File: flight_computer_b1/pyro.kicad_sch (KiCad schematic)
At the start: 11 parts, among them Q1 MMBT3904, Q2 PMOS, U11 IRLML6344TRPBF

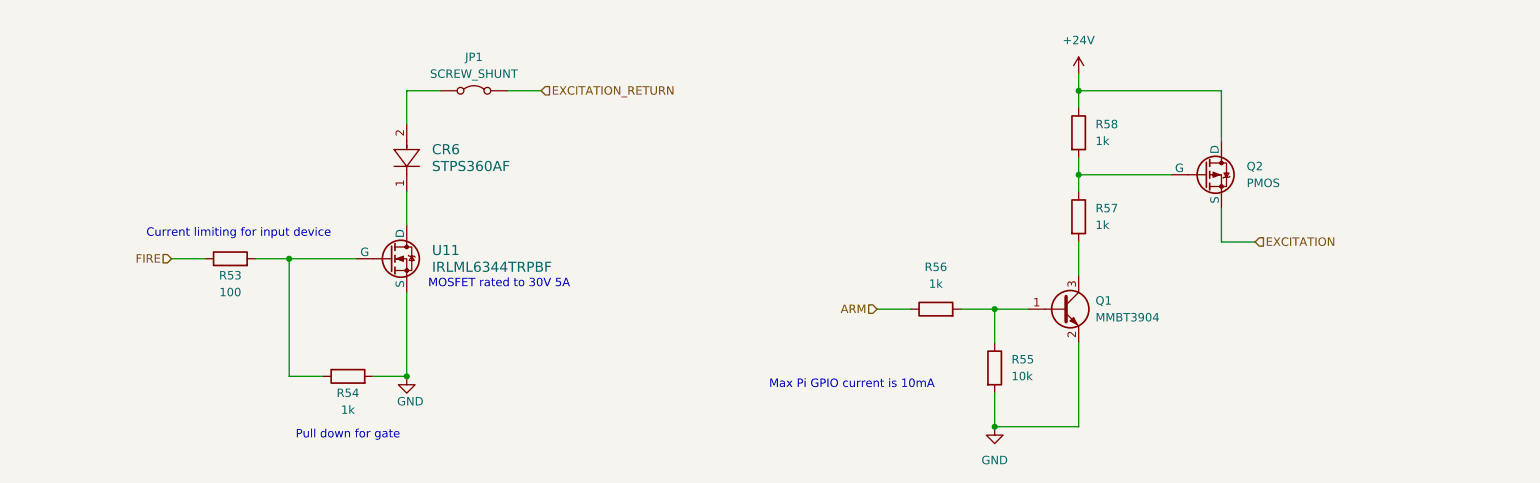
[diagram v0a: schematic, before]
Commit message: flight computer: new ideal diode, small schematic changes
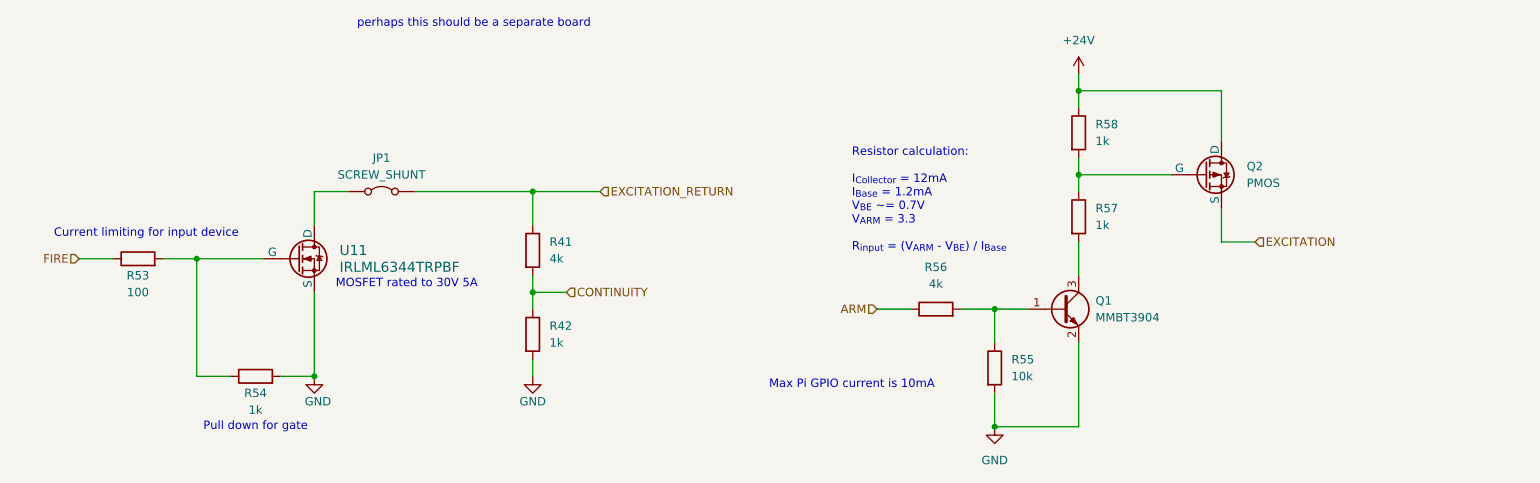
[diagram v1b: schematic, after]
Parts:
- removed CR6: STPS360AF, Diode_SMD:D_SOD-128, symbol MBRS360T3G:MBRS360T3G
- added R41: 4k, Resistor_SMD:R_0603_1608Metric, symbol Device:R
- added R42: 1k, Resistor_SMD:R_0603_1608Metric, symbol Device:R
- R56: value 1k -> 4k
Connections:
- net EXCITATION_RETURN: now also R41.1
- net GND: now also R42.2
- net at U11.1 (D): now also JP1.1 (A)
- new net CONTINUITY: R41.2, R42.1
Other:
- note added: "Resistor calculation: I_{Collector} = 12mA I_{Base} = 1.2mA V_{BE} ~= 0.7V V_{ARM} = 3.3 R_{input} = (V_{ARM} - V_{BE}) / I_{Base}"
- note added: "perhaps this should be a separate board"
- moved on the sheet: JP1, R53, R54, U11

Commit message: flight computer: routing updates
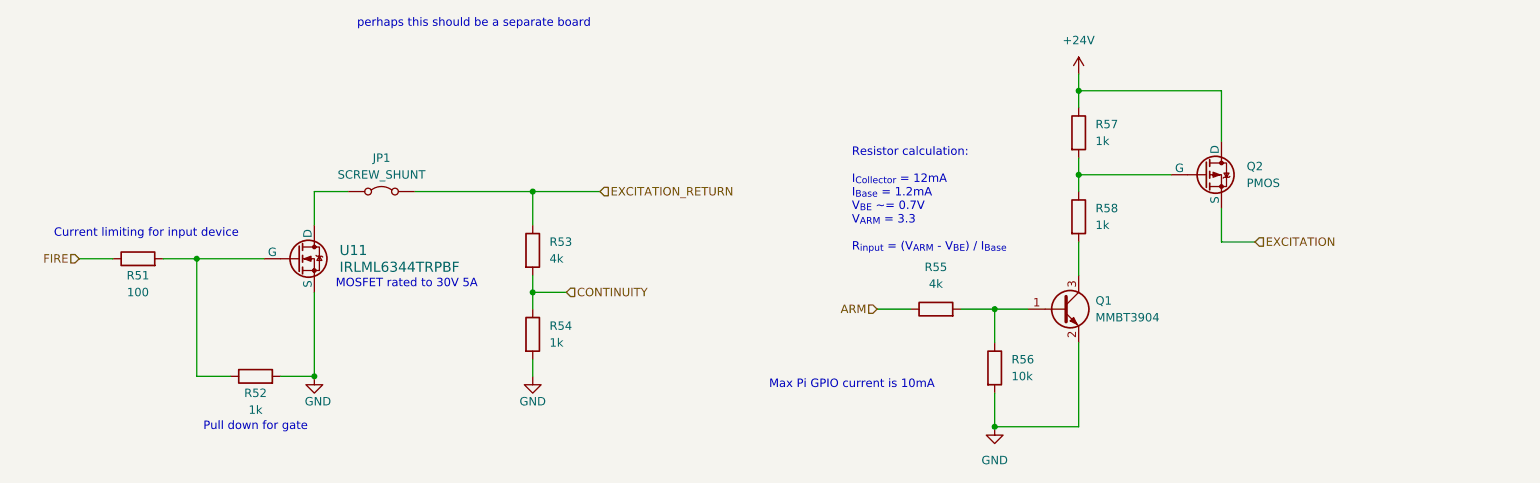
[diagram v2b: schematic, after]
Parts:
- R51: renamed from R53; DIGIKEY PART N (none) -> 541-100HCT-ND
- R55: renamed from R56; footprint (none) -> Resistor_SMD:R_0603_1608Metric
- R56: renamed from R55; footprint (none) -> Resistor_SMD:R_0603_1608Metric
- R57: renamed from R58; footprint (none) -> Resistor_SMD:R_0603_1608Metric
- R58: renamed from R57; footprint (none) -> Resistor_SMD:R_0603_1608Metric
- renumbered R54 to R52, R41 to R53, R42 to R54
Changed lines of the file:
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@@
 		(dnp no)
 		(fields_autoplaced yes)
-		(property "Reference" "R41"
+		(property "Reference" "R53"
 			(at 114.3 88.8999 0)
 			(effects
@@
 			(project "flight_computer"
 				(path "/b71a7b79-cdb5-4e38-a72c-0daaa3474f05/1be63f81-f9ac-4d7f-9cfb-3f22579c6b53"
-					(reference "R41")
+					(reference "R53")
 					(unit 1)
 				)
@@
 		(dnp no)
 		(fields_autoplaced yes)
-		(property "Reference" "R56"
+		(property "Reference" "R55"
 			(at 172.72 92.71 90)
 			(effects
@@
 			)
 		)
-		(property "Footprint" ""
+		(property "Footprint" "Resistor_SMD:R_0603_1608Metric"
 			(at 172.72 100.838 90)
 			(effects
@@
 			(project "flight_computer"
 				(path "/b71a7b79-cdb5-4e38-a72c-0daaa3474f05/1be63f81-f9ac-4d7f-9cfb-3f22579c6b53"
-					(reference "R56")
+					(reference "R55")
 					(unit 1)
 				)
@@
 		(on_board yes)
 		(dnp no)
-		(property "Reference" "R53"
+		(property "Reference" "R51"
 			(at 52.07 93.98 90)
 			(effects
@@
 			)
 		)
-		(property "DIGIKEY PART N" ""
+		(property "DIGIKEY PART N" "541-100HCT-ND"
 			(at 52.07 91.44 90)
 			(effects
@@
 			(project "flight_computer"
 				(path "/b71a7b79-cdb5-4e38-a72c-0daaa3474f05/1be63f81-f9ac-4d7f-9cfb-3f22579c6b53"
-					(reference "R53")
+					(reference "R51")
 					(unit 1)
 				)
@@
 		(dnp no)
 		(fields_autoplaced yes)
-		(property "Reference" "R58"
+		(property "Reference" "R57"
 			(at 196.85 71.1199 0)
 			(effects
@@
 			)
 		)
-		(property "Footprint" ""
+		(property "Footprint" "Resistor_SMD:R_0603_1608Metric"
 			(at 192.532 72.39 90)
 			(effects
@@
 			(project "flight_computer"
 				(path "/b71a7b79-cdb5-4e38-a72c-0daaa3474f05/1be63f81-f9ac-4d7f-9cfb-3f22579c6b53"
-					(reference "R58")
+					(reference "R57")
 					(unit 1)
 				)
@@
 		(dnp no)
 		(fields_autoplaced yes)
-		(property "Reference" "R57"
+		(property "Reference" "R58"
 			(at 196.85 83.8199 0)
 			(effects
@@
 			)
 		)
-		(property "Footprint" ""
+		(property "Footprint" "Resistor_SMD:R_0603_1608Metric"
 			(at 192.532 85.09 90)
 			(effects
@@
 			(project "flight_computer"
 				(path "/b71a7b79-cdb5-4e38-a72c-0daaa3474f05/1be63f81-f9ac-4d7f-9cfb-3f22579c6b53"
-					(reference "R57")
+					(reference "R58")
 					(unit 1)
 				)
@@
 		(dnp no)
 		(fields_autoplaced yes)
-		(property "Reference" "R42"
+		(property "Reference" "R54"
 			(at 114.3 101.5999 0)
 			(effects
@@
 			(project "flight_computer"
 				(path "/b71a7b79-cdb5-4e38-a72c-0daaa3474f05/1be63f81-f9ac-4d7f-9cfb-3f22579c6b53"
-					(reference "R42")
+					(reference "R54")
 					(unit 1)
 				)
@@
 		(dnp no)
 		(fields_autoplaced yes)
-		(property "Reference" "#PWR04"
+		(property "Reference" "#PWR071"
 			(at 194.31 67.31 0)
 			(effects
@@
 			(project ""
 				(path "/b71a7b79-cdb5-4e38-a72c-0daaa3474f05/1be63f81-f9ac-4d7f-9cfb-3f22579c6b53"
-					(reference "#PWR04")
+					(reference "#PWR071")
 					(unit 1)
 				)
@@
 		(on_board yes)
 		(dnp no)
-		(property "Reference" "#PWR02"
+		(property "Reference" "#PWR068"
 			(at 78.74 115.57 0)
 			(effects
@@
 			(project "flight_computer"
 				(path "/b71a7b79-cdb5-4e38-a72c-0daaa3474f05/1be63f81-f9ac-4d7f-9cfb-3f22579c6b53"
-					(reference "#PWR02")
+					(reference "#PWR068")
 					(unit 1)
 				)
@@
 		(on_board yes)
 		(dnp no)
-		(property "Reference" "R54"
+		(property "Reference" "R52"
 			(at 69.85 111.76 90)
 			(effects
@@
 			(project "flight_computer"
 				(path "/b71a7b79-cdb5-4e38-a72c-0daaa3474f05/1be63f81-f9ac-4d7f-9cfb-3f22579c6b53"
-					(reference "R54")
+					(reference "R52")
 					(unit 1)
 				)
@@
 		(on_board yes)
 		(dnp no)
-		(property "Reference" "#PWR08"
+		(property "Reference" "#PWR069"
 			(at 111.76 115.57 0)
 			(effects
@@
 			(project "flight_computer"
 				(path "/b71a7b79-cdb5-4e38-a72c-0daaa3474f05/1be63f81-f9ac-4d7f-9cfb-3f22579c6b53"
-					(reference "#PWR08")
+					(reference "#PWR069")
 					(unit 1)
 				)
@@
 		(dnp no)
 		(fields_autoplaced yes)
-		(property "Reference" "R55"
+		(property "Reference" "R56"
 			(at 184.15 106.6799 0)
 			(effects
@@
 			)
 		)
-		(property "Footprint" ""
+		(property "Footprint" "Resistor_SMD:R_0603_1608Metric"
 			(at 179.832 107.95 90)
 			(effects
@@
 			(project ""
 				(path "/b71a7b79-cdb5-4e38-a72c-0daaa3474f05/1be63f81-f9ac-4d7f-9cfb-3f22579c6b53"
-					(reference "R55")
+					(reference "R56")
 					(unit 1)
 				)
@@
 		(dnp no)
 		(fields_autoplaced yes)
-		(property "Reference" "#PWR03"
+		(property "Reference" "#PWR070"
 			(at 181.61 123.19 0)
 			(effects
@@
 			(project ""
 				(path "/b71a7b79-cdb5-4e38-a72c-0daaa3474f05/1be63f81-f9ac-4d7f-9cfb-3f22579c6b53"
-					(reference "#PWR03")
-					(unit 1)
-				)
+					(reference "#PWR070")
+					(unit 1)
+				)

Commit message: flight computer: new pyro circuit
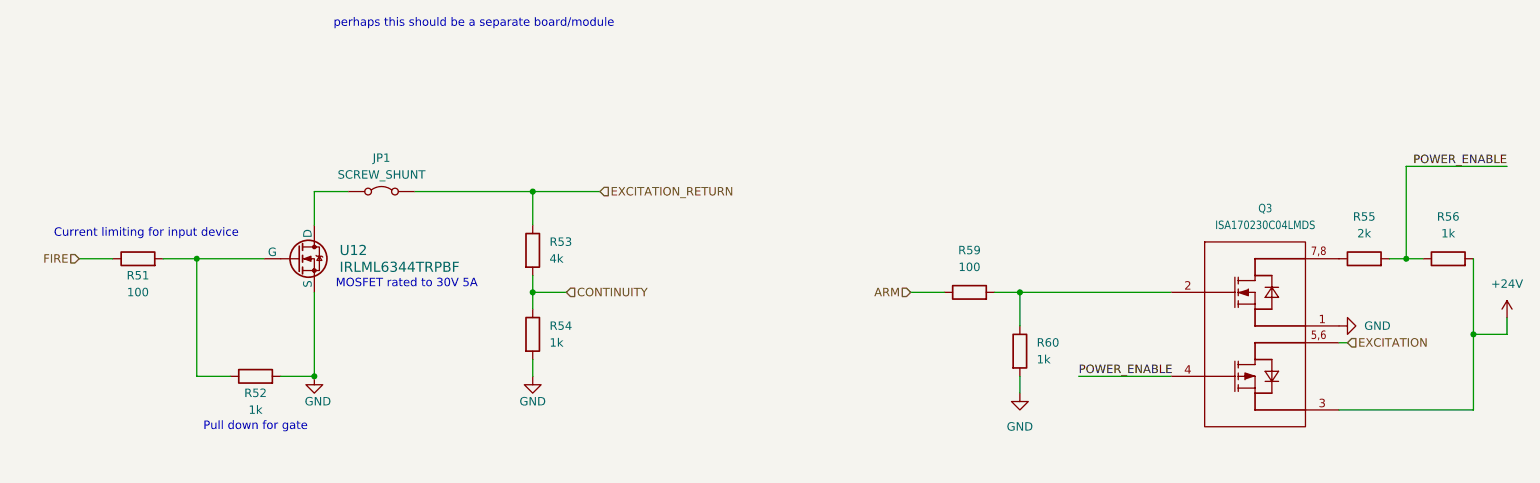
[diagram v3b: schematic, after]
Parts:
- removed Q1: MMBT3904, Package_TO_SOT_SMD:SOT-23, symbol Transistor_BJT:MMBT3904
- removed Q2: PMOS, symbol Simulation_SPICE:PMOS
- removed R57, R58: 1k, Resistor_SMD:R_0603_1608Metric, symbol Device:R
- added Q3: ISA170230C04LMDS, avi_lib:PG-DSO-8-920-V, symbol avi_lib:ISA170230C04LMDS
- added R59: 100, Resistor_SMD:R_0603_1608Metric, symbol Device:R
- added R60: 1k, Resistor_SMD:R_0603_1608Metric, symbol Device:R
- R55: value 4k -> 2k
- R56: value 10k -> 1k
- renumbered U11 to U12
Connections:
- net +24V: now also R56.2, Q3.3
- net ARM: now also R59.1; no longer R55.1
- net EXCITATION: now also Q3.5, Q3.6
- net GND: now also Q3.1, R60.2; no longer R56.2
- net POWER_ENABLE: now reaches R55.2, R56.1
- net POWER_ENABLE: now also Q3.4
- new net: Q3.2, R59.2, R60.1
- new net: Q3.7, Q3.8, R55.1
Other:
- note added: "perhaps this should be a separate board/module"
- note removed: "Max Pi GPIO current is 10mA"
- note removed: "Resistor calculation: I_{Collector} = 12mA I_{Base} = 1.2mA V_{BE} ~= 0.7V V_{ARM} = 3.3 R_{input} = (V_{ARM} - V_{BE}) / I_{Base}"
- note removed: "perhaps this should be a separate board"

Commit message: routed pi traces, fixed all unavoidable DRC errors
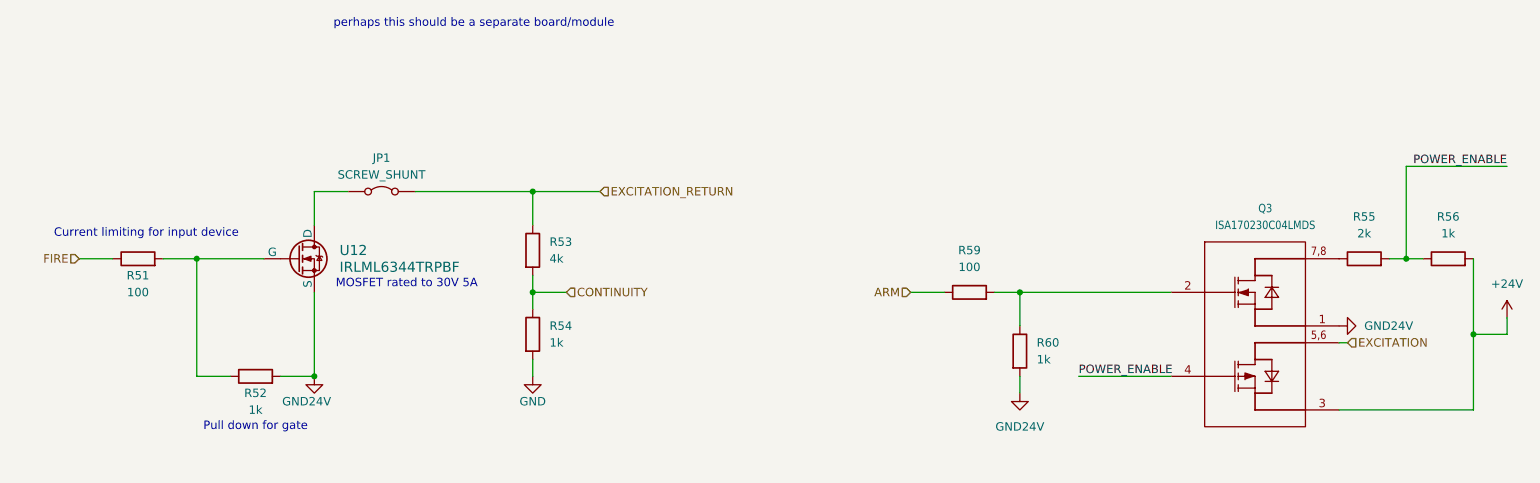
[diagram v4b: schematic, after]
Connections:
- net GND: no longer Q3.1, R52.2, R60.2, U12.3 (S)
- new net GND24V: Q3.1, R52.2, R60.2, U12.3 (S)
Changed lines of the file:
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@@
 			)
 		)
-		(property "Value" "GND"
+		(property "Value" "GND24V"
 			(at 81.28 113.03 0)
 			(effects
@@
 			)
 		)
-		(property "Value" "GND"
+		(property "Value" "GND24V"
 			(at 237.49 101.5999 90)
 			(effects
@@
 			)
 		)
-		(property "Value" "GND"
+		(property "Value" "GND24V"
 			(at 185.42 116.84 0)
 			(effects
